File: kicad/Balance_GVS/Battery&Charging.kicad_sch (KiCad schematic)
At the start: 26 parts, among them J2 USB_C_Receptacle, SW2 SW_SPDT, U5 TPS7A4901DGNT, U7 MT3608, U8 TP4056

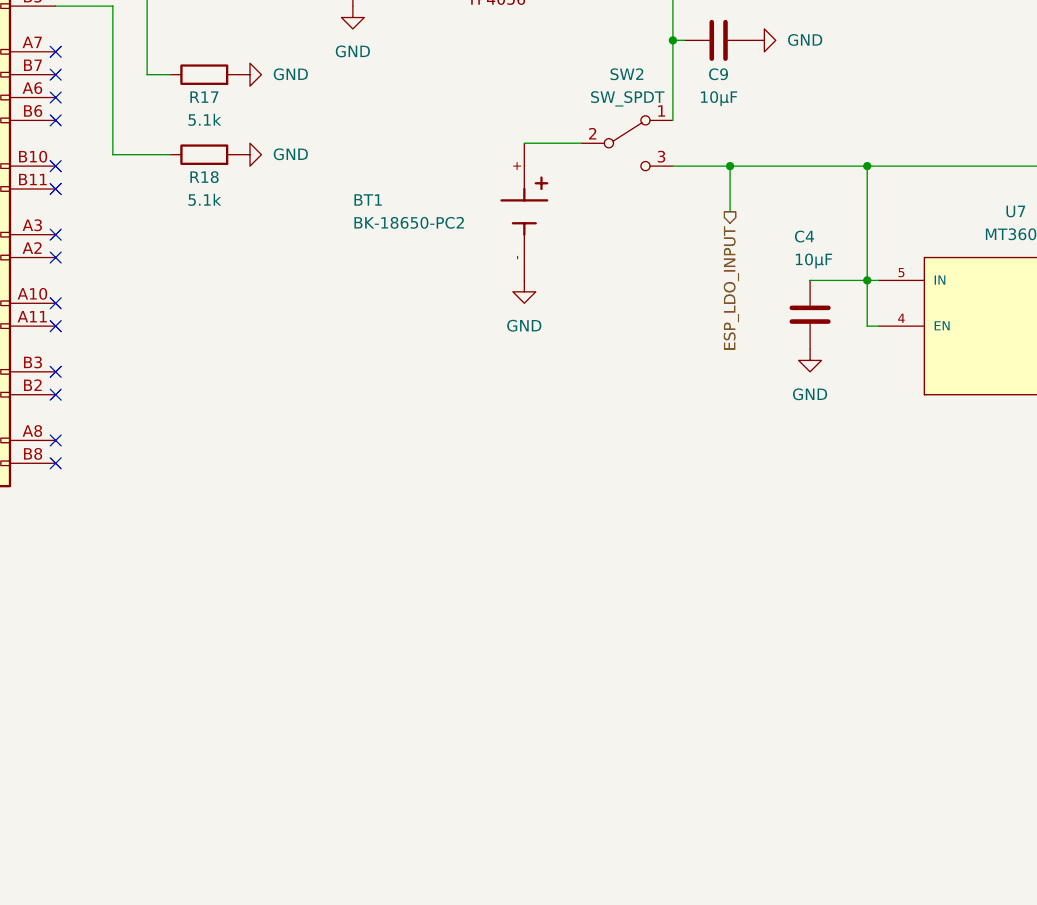
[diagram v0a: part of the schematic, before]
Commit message: Add 3.3V Voltage Regulator and ESP32 Battery ADC
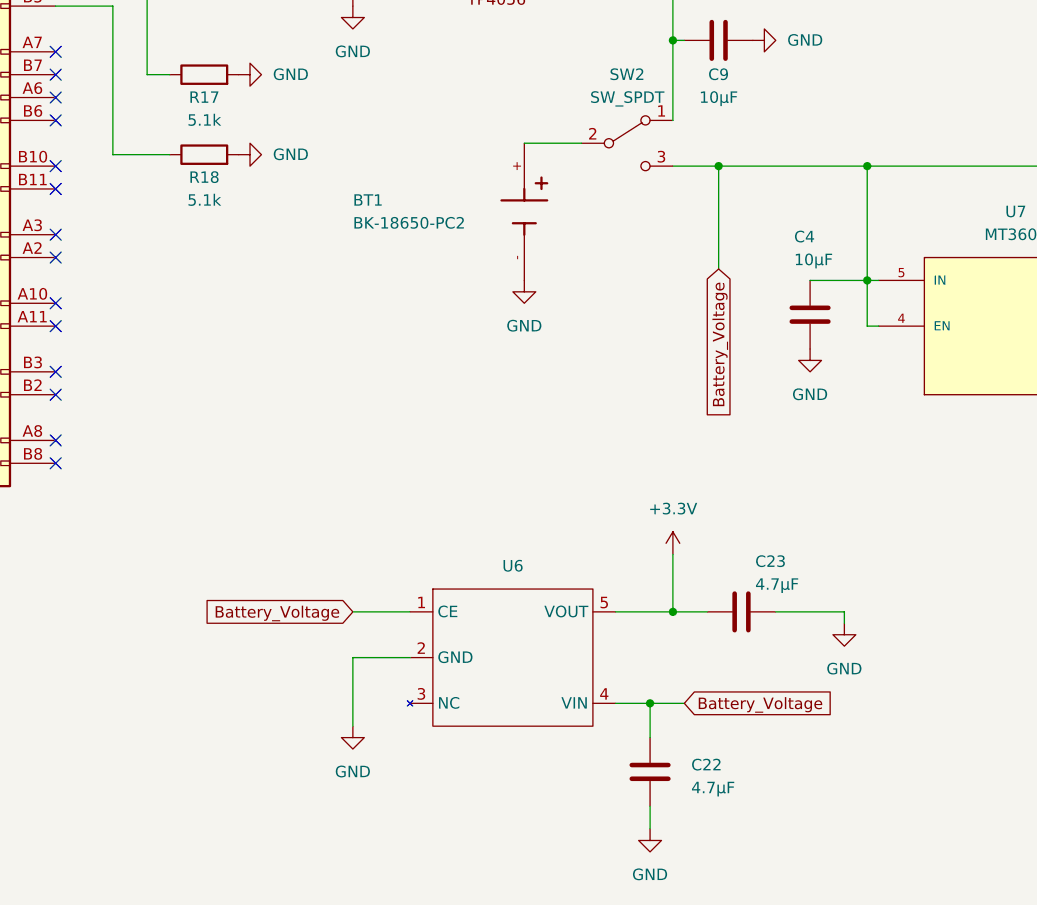
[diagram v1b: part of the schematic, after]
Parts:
- added C22, C23: 4.7µF, symbol Device:C
- added U6: (no value), Package_TO_SOT_SMD:SOT-89-5_Handsoldering, symbol GVS_Library:R1172H331B-T1-FE
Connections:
- net GND: now also C22.2, C23.1, U6.2 (GND)
- net ESP_LDO_INPUT renamed Battery_Voltage
- net Battery_Voltage: now also C22.1, U6.1 (CE), U6.4 (VIN)
- new net +3.3V: C23.2, U6.5 (VOUT)

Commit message: Started adding howland connections
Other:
- moved on the sheet: R17, R18
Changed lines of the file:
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@@
 	(wire
 		(pts
-			(xy 52.07 99.06) (xy 58.42 99.06)
-		)
-		(stroke
-			(width 0)
-			(type default)
-		)
-	)
-	(wire
-		(pts
 			(xy 210.82 82.55) (xy 210.82 97.79)
 		)
@@
 	(wire
 		(pts
-			(xy 55.88 90.17) (xy 55.88 80.01)
+			(xy 45.72 74.93) (xy 60.96 74.93)
 		)
 		(stroke
@@
 	(wire
 		(pts
-			(xy 45.72 74.93) (xy 60.96 74.93)
+			(xy 45.72 82.55) (xy 57.15 82.55)
 		)
 		(stroke
@@
 	(wire
 		(pts
-			(xy 114.3 149.86) (xy 118.11 149.86)
+			(xy 45.72 80.01) (xy 67.31 80.01)
 		)
 		(stroke
@@
 	(wire
 		(pts
-			(xy 167.64 100.33) (xy 167.64 113.03)
+			(xy 114.3 149.86) (xy 118.11 149.86)
 		)
 		(stroke
@@
 	(wire
 		(pts
-			(xy 78.74 154.94) (xy 85.09 154.94)
+			(xy 167.64 100.33) (xy 167.64 113.03)
 		)
 		(stroke
@@
 	(wire
 		(pts
-			(xy 114.3 59.69) (xy 118.11 59.69)
+			(xy 78.74 154.94) (xy 85.09 154.94)
 		)
 		(stroke
@@
 	(wire
 		(pts
-			(xy 52.07 99.06) (xy 52.07 82.55)
+			(xy 114.3 59.69) (xy 118.11 59.69)
 		)
 		(stroke
@@
 	(wire
 		(pts
-			(xy 58.42 90.17) (xy 55.88 90.17)
-		)
-		(stroke
-			(width 0)
-			(type default)
-		)
-	)
-	(wire
-		(pts
 			(xy 135.89 118.11) (xy 135.89 113.03)
 		)
@@
 	(wire
 		(pts
-			(xy 52.07 82.55) (xy 45.72 82.55)
-		)
-		(stroke
-			(width 0)
-			(type default)
-		)
-	)
-	(wire
-		(pts
 			(xy 78.74 149.86) (xy 85.09 149.86)
 		)
@@
 	(wire
 		(pts
-			(xy 55.88 80.01) (xy 45.72 80.01)
-		)
-		(stroke
-			(width 0)
-			(type default)
-		)
-	)
-	(wire
-		(pts
 			(xy 208.28 100.33) (xy 210.82 100.33)
 		)
@@
 		)
 	)
+	(global_label "Howland_Supply_Rail"
+		(shape output)
+		(at 259.08 97.79 0)
+		(fields_autoplaced yes)
+		(effects
+			(font
+				(size 1.27 1.27)
+			)
+			(justify left)
+		)
+		(property "Intersheetrefs" "${INTERSHEET_REFS}"
+			(at 281.9009 97.79 0)
+			(hide yes)
+			(show_name no)
+			(do_not_autoplace no)
+			(effects
+				(font
+					(size 1.27 1.27)
+				)
+				(justify left)
+			)
+		)
+	)
 	(global_label "Battery_Voltage"
-		(shape input)
+		(shape output)
 		(at 119.38 111.76 270)
 		(fields_autoplaced yes)
@@
 		)
 	)
-	(hierarchical_label "Howland_Supply_Rail"
-		(shape output)
-		(at 259.08 97.79 0)
-		(effects
-			(font
-				(size 1.27 1.27)
-			)
-			(justify left)
-		)
-	)
 	(symbol
 		(lib_id "Device:R")
@@
 	(symbol
 		(lib_id "power:GND")
-		(at 66.04 90.17 90)
+		(at 67.31 87.63 0)
 		(unit 1)
 		(body_style 1)
@@
 		(fields_autoplaced yes)
 		(property "Reference" "#PWR034"
-			(at 72.39 90.17 0)
+			(at 67.31 93.98 0)
 			(hide yes)
 			(show_name no)
@@
 		)
 		(property "Value" "GND"
-			(at 69.85 90.17 90)
+			(at 67.31 91.44 90)
 			(show_name no)
 			(do_not_autoplace no)
@@
 		)
 		(property "Footprint" ""
-			(at 66.04 90.17 0)
+			(at 67.31 87.63 0)
 			(hide yes)
 			(show_name no)
@@
 		)
 		(property "Datasheet" ""
-			(at 66.04 90.17 0)
+			(at 67.31 87.63 0)
 			(hide yes)
 			(show_name no)
@@
 		)
 		(property "Description" ""
-			(at 66.04 90.17 0)
+			(at 67.31 87.63 0)
 			(show_name no)
 			(do_not_autoplace no)
@@
 	(symbol
 		(lib_id "Device:R")
-		(at 62.23 99.06 90)
+		(at 57.15 86.36 0)
 		(unit 1)
 		(body_style 1)
@@
 		(dnp no)
 		(property "Reference" "R18"
-			(at 62.23 101.6 90)
+			(at 53.34 87.63 0)
 			(show_name no)
 			(do_not_autoplace no)
@@
 		)
 		(property "Value" "5.1k"
-			(at 62.23 104.14 90)
+			(at 53.34 85.09 0)
 			(show_name no)
 			(do_not_autoplace no)
@@
 		)
 		(property "Footprint" ""
-			(at 62.23 100.838 90)
+			(at 55.372 86.36 90)
 			(hide yes)
 			(show_name no)
@@
 		)
 		(property "Datasheet" ""
-			(at 62.23 99.06 0)
+			(at 57.15 86.36 0)
 			(hide yes)
 			(show_name no)
@@
 		)
 		(property "Description" ""
-			(at 62.23 99.06 0)
+			(at 57.15 86.36 0)
 			(show_name no)
 			(do_not_autoplace no)
@@
 	(symbol
 		(lib_id "power:GND")
-		(at 66.04 99.06 90)
+		(at 57.15 90.17 0)
 		(unit 1)
 		(body_style 1)
@@
 		(fields_autoplaced yes)
 		(property "Reference" "#PWR035"
-			(at 72.39 99.06 0)
+			(at 57.15 96.52 0)
 			(hide yes)
 			(show_name no)
@@
 		)
 		(property "Value" "GND"
-			(at 69.85 99.06 90)
+			(at 57.15 93.98 90)
 			(show_name no)
 			(do_not_autoplace no)
@@
 		)
 		(property "Footprint" ""
-			(at 66.04 99.06 0)
+			(at 57.15 90.17 0)
 			(hide yes)
 			(show_name no)
@@
 		)
 		(property "Datasheet" ""
-			(at 66.04 99.06 0)
+			(at 57.15 90.17 0)
 			(hide yes)
 			(show_name no)
@@
 		)
 		(property "Description" ""
-			(at 66.04 99.06 0)
+			(at 57.15 90.17 0)
 			(show_name no)
 			(do_not_autoplace no)
@@
 	(symbol
 		(lib_id "Device:R")
-		(at 62.23 90.17 90)
+		(at 67.31 83.82 0)
 		(unit 1)
 		(body_style 1)
@@
 		(dnp no)
 		(property "Reference" "R17"
-			(at 62.23 92.71 90)
+			(at 63.5 85.09 0)
 			(show_name no)
 			(do_not_autoplace no)
@@
 		)
 		(property "Value" "5.1k"
-			(at 62.23 95.25 90)
+			(at 63.5 82.55 0)
 			(show_name no)
 			(do_not_autoplace no)
@@
 		)
 		(property "Footprint" ""
-			(at 62.23 91.948 90)
+			(at 65.532 83.82 90)
 			(hide yes)
 			(show_name no)
@@
 		)
 		(property "Datasheet" ""
-			(at 62.23 90.17 0)
+			(at 67.31 83.82 0)
 			(hide yes)
 			(show_name no)
@@
 		)
 		(property "Description" ""
-			(at 62.23 90.17 0)
+			(at 67.31 83.82 0)
 			(show_name no)
 			(do_not_autoplace no)

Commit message: Finish Howland
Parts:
- removed C22, C23: 4.7µF, symbol Device:C
- removed U6: (no value), Package_TO_SOT_SMD:SOT-89-5_Handsoldering, symbol GVS_Library:R1172H331B-T1-FE
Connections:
- net Howland_Supply_Rail renamed 24V

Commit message: Add Footprints to Schematic
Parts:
- removed D4: MBR0540, Diode_SMD:D_SOD-123, symbol Diode:MBR0540
- removed SW2: SW_SPDT, symbol Switch:SW_SPDT
- added D9: SS14, Diode_SMD:D_SMA, symbol Diode:SS14
- added J3, J4: Conn_01x02_Pin, Connector_PinSocket_2.54mm:PinSocket_1x02_P2.54mm_Vertical, symbol Connector:Conn_01x02_Pin
- added SW7: SS-12D00-G 4 E, ul_SS-12D00-G-4-E:1P2T_SS-12D00_CNK, symbol ul_SS-12D00-G-4-E:SS-12D00-G_4_E
- BT1: footprint BK_18650_PC2:BAT_BK-18650-PC2 -> FreddyBattery:BH-18650-B1BA002
- C10, C4, C5, C6, C7, C8, C9: footprint (none) -> Capacitor_SMD:C_0805_2012Metric_Pad1.18x1.45mm_HandSolder
- D1, D2: footprint (none) -> LED_SMD:LED_0603_1608Metric_Pad1.05x0.95mm_HandSolder
- J2: footprint (none) -> USB4105_GF_A:USB4105_GCT
- L1: footprint (none) -> SRN4018_4R7M:IND_BOURNS_SRN4018
- R12, R13, R14, R15, R16, R17, R18, R19, R20: footprint (none) -> Resistor_SMD:R_0805_2012Metric_Pad1.20x1.40mm_HandSolder
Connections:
- net 24V: now also J4.2 (Pin_2)
- net Battery_Voltage: now also J3.2 (Pin_2), SW7.3
- net GND: now also J3.1 (Pin_1), J4.1 (Pin_1)
- net at C10.1, C5.1, R19.1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: now also D9.1 (K)
- net at L1.1, U7.1 (SW): now also D9.2 (A)
- net at C9.1, U8.5 (BAT): now also SW7.1
- net at BT1.+: now also SW7.2
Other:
- moved on the sheet: BT1
